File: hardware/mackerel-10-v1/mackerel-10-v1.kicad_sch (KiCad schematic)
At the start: 14 parts, among them J1 Conn_02x05_Odd_Even, J2 DIN41612_02x32_AC, U1 68010D, X1 50 MHz

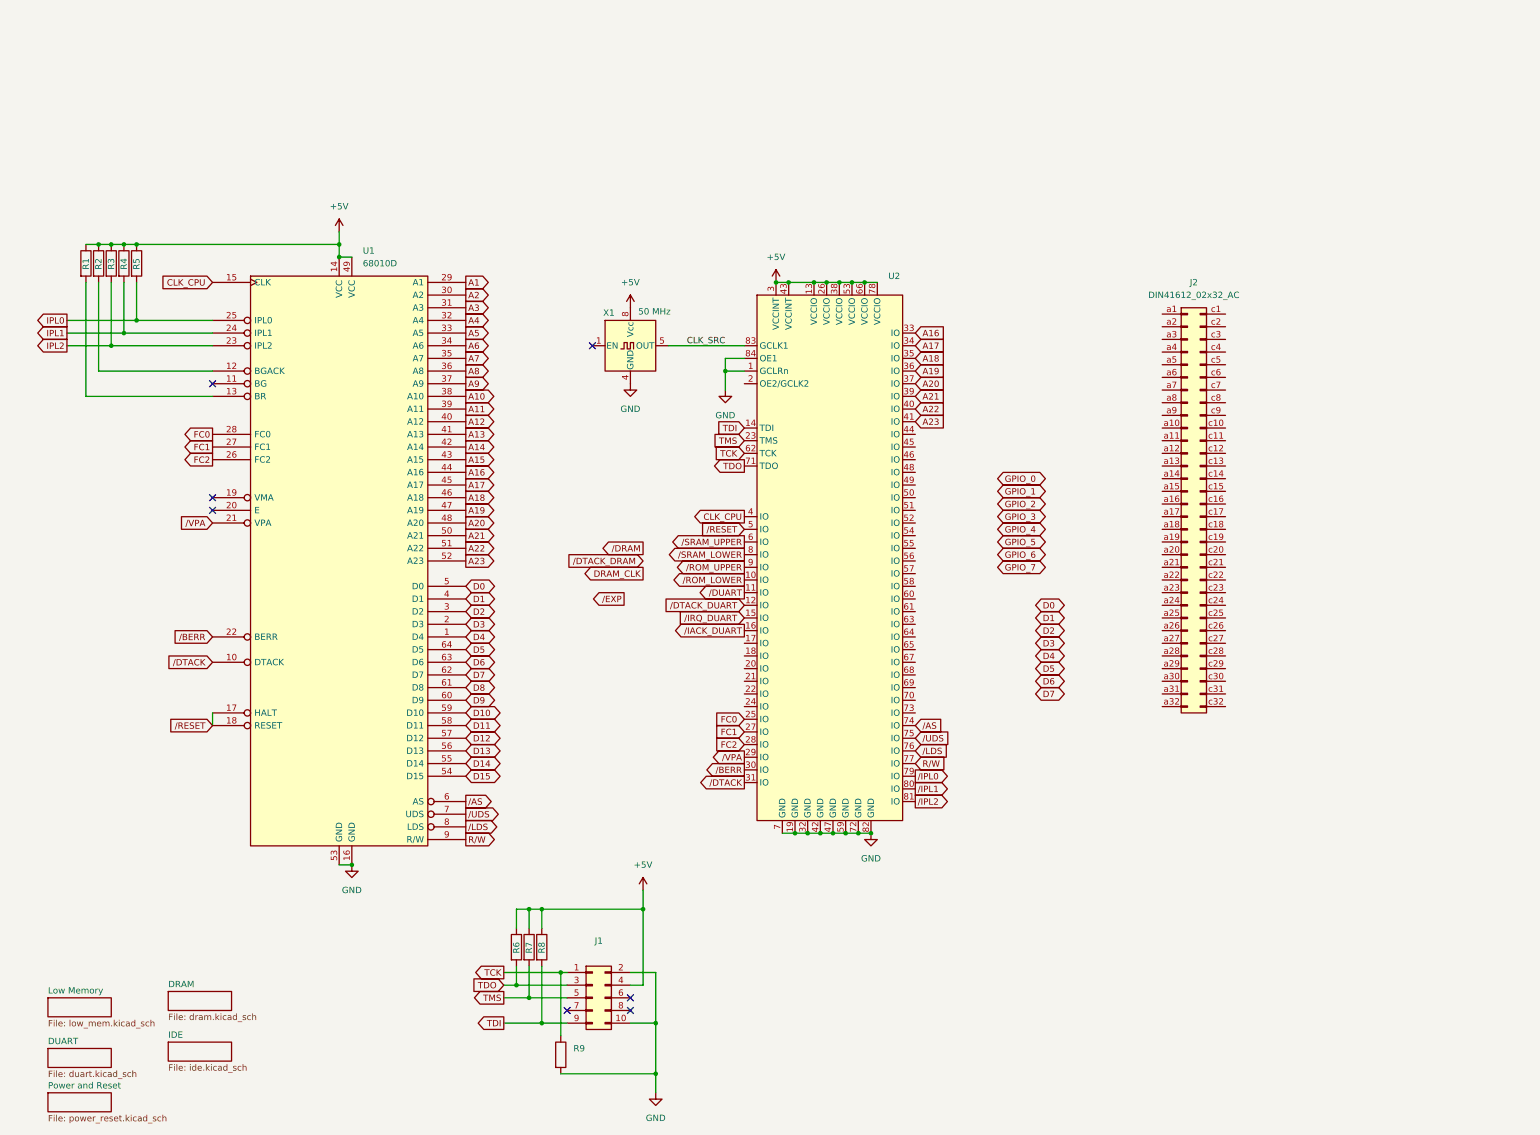
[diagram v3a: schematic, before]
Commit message: Rough layout of simplified Mack-10 prototype
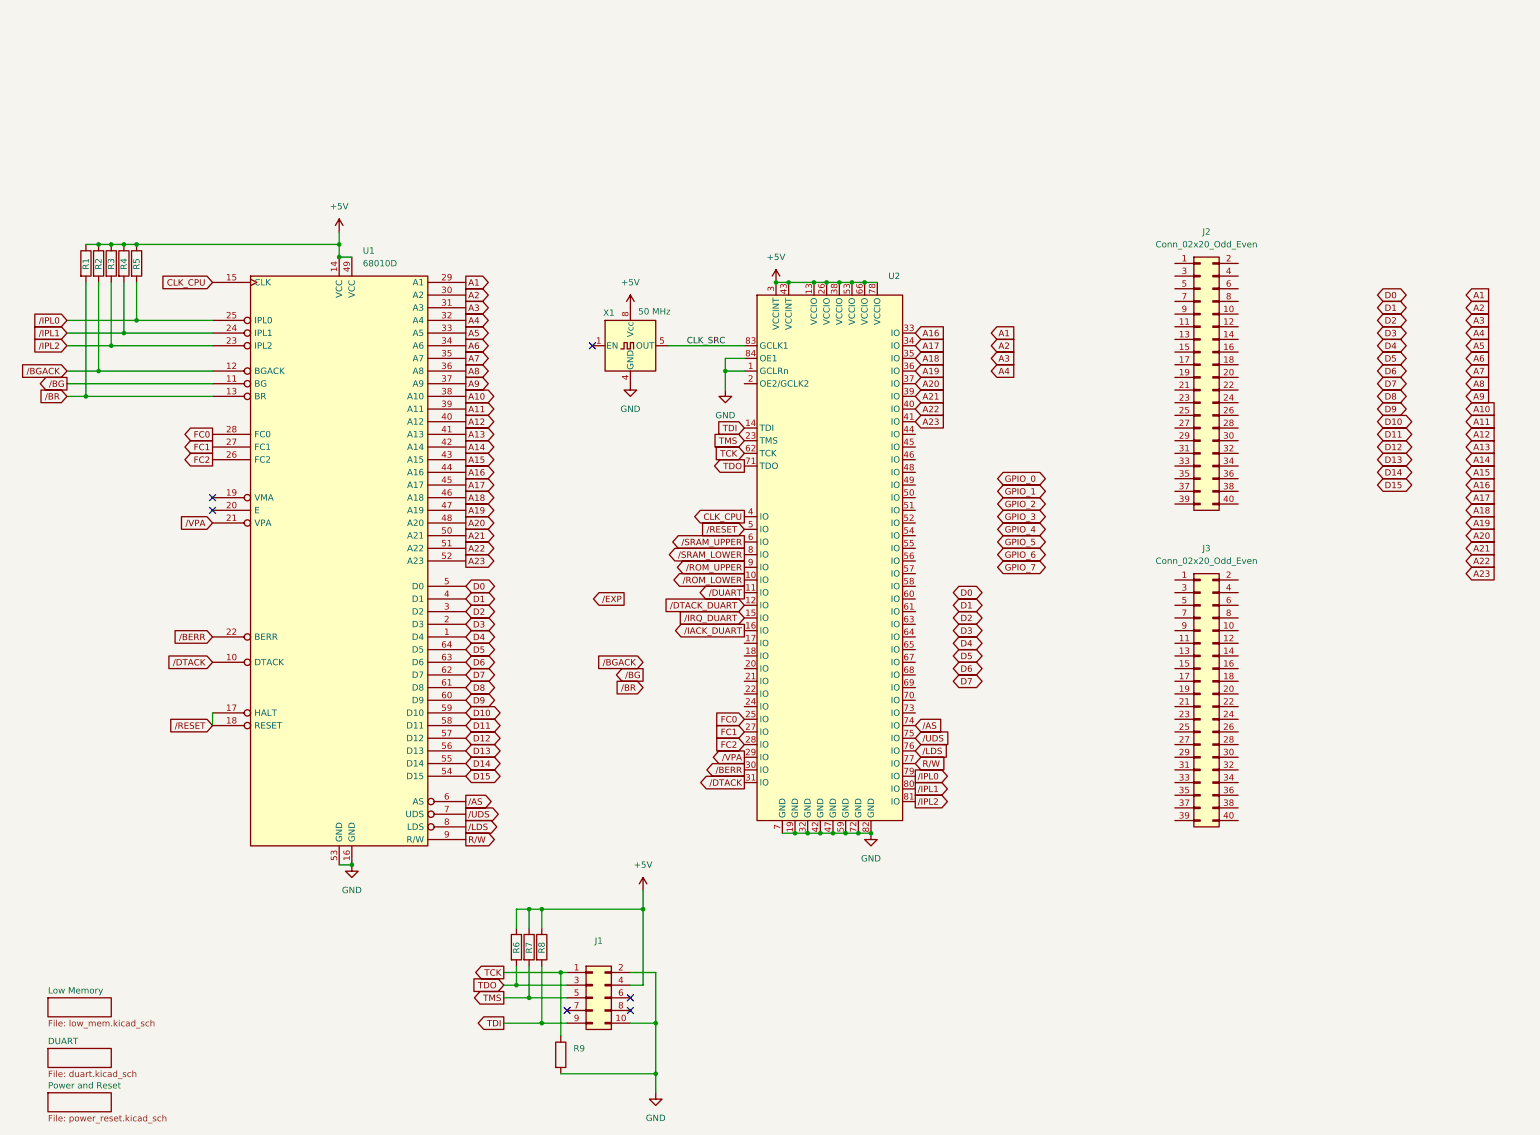
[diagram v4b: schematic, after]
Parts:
- removed J2: DIN41612_02x32_AC, Connector_DIN:DIN41612_C_2x32_Female_Vertical_THT, symbol Connector:DIN41612_02x32_AC
- added J2, J3: Conn_02x20_Odd_Even, Connector_IDC:IDC-Header_2x20_P2.54mm_Vertical, symbol Connector_Generic:Conn_02x20_Odd_Even
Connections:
- net IPL0 is gone; now on net /IPL0: R5.2, U1.25 (IPL0)
- net IPL1 is gone; now on net /IPL1: R4.2, U1.24 (IPL1)
- net IPL2 is gone; now on net /IPL2: R3.2, U1.23 (IPL2)
- net /BG: now reaches U1.11 (BG)
- net /BGACK: now reaches R2.2, U1.12 (BGACK)
- net /BR: now reaches R1.2, U1.13 (BR)
- no-connect marks 7 -> 6
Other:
- removed sheet DRAM
- removed sheet IDE

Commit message: Mack-10 proto routed except for expansion headers
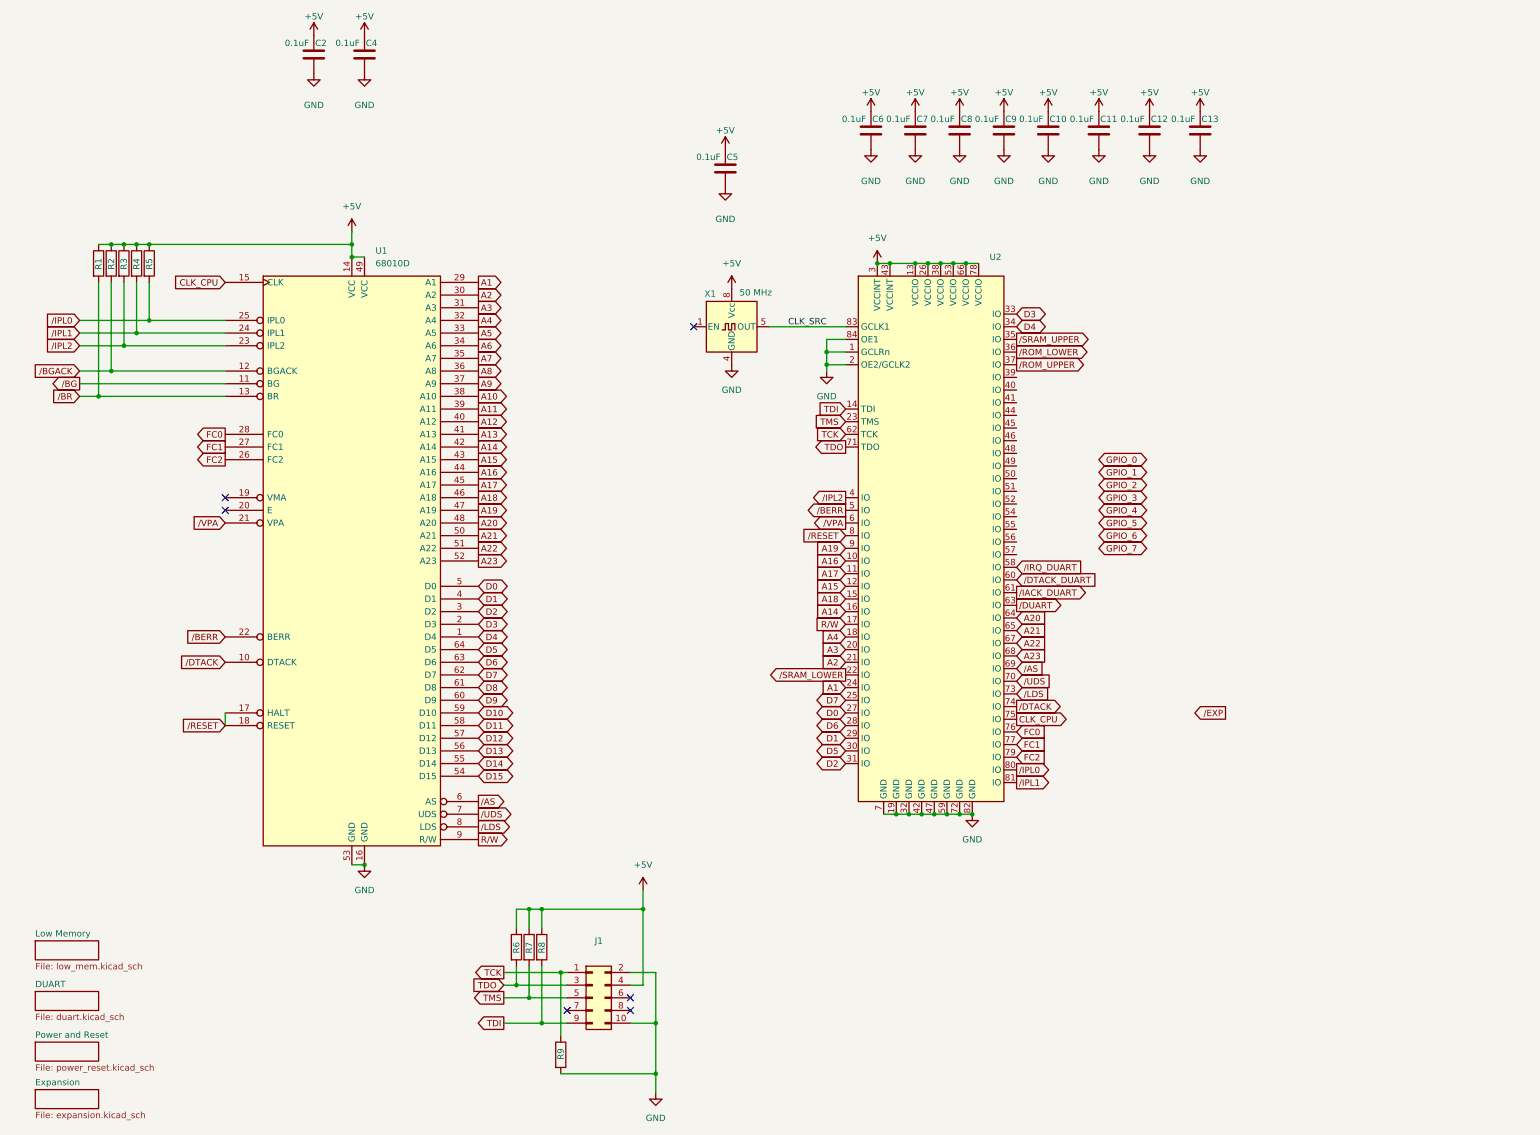
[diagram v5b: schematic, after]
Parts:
- removed J2, J3: Conn_02x20_Odd_Even, Connector_IDC:IDC-Header_2x20_P2.54mm_Vertical, symbol Connector_Generic:Conn_02x20_Odd_Even
- added C10, C11, C12, C13, C2, C4, C5, C6, C7, C8, C9: 0.1uF, Capacitor_THT:C_Disc_D4.7mm_W2.5mm_P5.00mm, symbol Device:C
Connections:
- net +5V: now also C10.1, C11.1, C12.1, C13.1, C2.1, C4.1, C5.1, C6.1, C7.1, C8.1, C9.1
- net A1: now also U2.24 (IO)
- net A14: now also U2.16 (IO)
- net A15: now also U2.12 (IO)
- net A16: now also U2.10 (IO); no longer U2.33 (IO)
- net A17: now also U2.11 (IO); no longer U2.34 (IO)
- net A18: now also U2.15 (IO); no longer U2.35 (IO)
- net A19: now also U2.9 (IO); no longer U2.36 (IO)
- net A2: now also U2.21 (IO)
- net A20: now also U2.64 (IO); no longer U2.37 (IO)
- net A21: now also U2.65 (IO); no longer U2.39 (IO)
- net A22: now also U2.67 (IO); no longer U2.40 (IO)
- net A23: now also U2.68 (IO); no longer U2.41 (IO)
- net A3: now also U2.20 (IO)
- net A4: now also U2.18 (IO)
- net CLK_CPU: now also U2.75 (IO); no longer U2.4 (IO)
- net D0: now also U2.27 (IO)
- net D1: now also U2.29 (IO)
- net D2: now also U2.31 (IO)
- net D3: now also U2.33 (IO)
- net D4: now also U2.34 (IO)
- net D5: now also U2.30 (IO)
- net D6: now also U2.28 (IO)
- net D7: now also U2.25 (IO)
- net FC0: now also U2.76 (IO); no longer U2.25 (IO)
- net FC1: now also U2.77 (IO); no longer U2.27 (IO)
- net FC2: now also U2.79 (IO); no longer U2.28 (IO)
- net GND: now also U2.2 (OE2/GCLK2), C10.2, C11.2, C12.2, C13.2, C2.2, C4.2, C5.2, C6.2, C7.2, C8.2, C9.2
- net R/W: now also U2.17 (IO); no longer U2.77 (IO)
- net /AS: now also U2.69 (IO); no longer U2.74 (IO)
- net /BERR: now also U2.5 (IO); no longer U2.30 (IO)
- net /DTACK: now also U2.74 (IO); no longer U2.31 (IO)
- net /DTACK_DUART: now also U2.60 (IO); no longer U2.12 (IO)
- net /DUART: now also U2.63 (IO); no longer U2.11 (IO)
- net /IACK_DUART: now also U2.61 (IO); no longer U2.16 (IO)
- net /IPL0: now also U2.80 (IO); no longer U2.79 (IO)
- net /IPL1: now also U2.81 (IO); no longer U2.80 (IO)
- net /IPL2: now also U2.4 (IO); no longer U2.81 (IO)
- net /IRQ_DUART: now also U2.58 (IO); no longer U2.15 (IO)
- net /LDS: now also U2.73 (IO); no longer U2.76 (IO)
- net /RESET: now also U2.8 (IO); no longer U2.5 (IO)
- net /ROM_LOWER: now also U2.36 (IO); no longer U2.10 (IO)
- net /ROM_UPPER: now also U2.37 (IO); no longer U2.9 (IO)
- net /SRAM_LOWER: now also U2.22 (IO); no longer U2.8 (IO)
- net /SRAM_UPPER: now also U2.35 (IO); no longer U2.6 (IO)
- net /UDS: now also U2.70 (IO); no longer U2.75 (IO)
- net /VPA: now also U2.6 (IO); no longer U2.29 (IO)
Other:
- added sheet Expansion (expansion.kicad_sch)
- moved on the sheet: R1, R2, R3, R4, R5, U1, U2, X1

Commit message: Mack-10 proto fully routed
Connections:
- net GPIO_0: now also U2.46 (IO)
- net GPIO_1: now also U2.45 (IO)
- net GPIO_2: now also U2.48 (IO)
- net GPIO_3: now also U2.49 (IO)
- net GPIO_4: now also U2.50 (IO)
- net GPIO_5: now also U2.51 (IO)
- net GPIO_6: now also U2.52 (IO)
- net GPIO_7: now also U2.54 (IO)
- net /EXP: now also U2.40 (IO)
- net /IRQ_EXP: now reaches U2.39 (IO)
- net /IACK_EXP: now reaches U2.41 (IO)
- net /DTACK_EXP: now reaches U2.44 (IO)
- net /BG: no longer names the net of U1.11 (BG)
- net /BGACK: no longer names the net of R2.2, U1.12 (BGACK)
- net /BR: no longer names the net of R1.2, U1.13 (BR)
- no-connect marks 6 -> 9
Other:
- note added: "TODO: extra chip select, DTACK, and IRQ/IACK pins"
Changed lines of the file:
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@@
 	)
 	(junction
+		(at 177.8 40.64)
+		(diameter 0)
+		(color 0 0 0 0)
+	)
+	(junction
 		(at 191.77 27.94)
 		(diameter 0)
@@
 	)
 	(no_connect
+		(at 212.09 86.36)
+	)
+	(no_connect
+		(at 212.09 81.28)
+	)
+	(no_connect
 		(at 134.62 175.26)
 	)
@@
 		(at 121.92 177.8)
 	)
+	(no_connect
+		(at 212.09 83.82)
+	)
 	(wire
 		(pts
@@
 	(wire
 		(pts
-			(xy 24.13 52.07) (xy 53.34 52.07)
+			(xy 33.02 44.45) (xy 53.34 44.45)
 		)
 		(stroke
@@
 	(wire
 		(pts
-			(xy 33.02 44.45) (xy 53.34 44.45)
+			(xy 198.12 138.43) (xy 200.66 138.43)
 		)
 		(stroke
@@
 	(wire
 		(pts
-			(xy 198.12 138.43) (xy 200.66 138.43)
+			(xy 109.22 175.26) (xy 114.3 175.26)
 		)
 		(stroke
@@
 	(wire
 		(pts
-			(xy 109.22 175.26) (xy 114.3 175.26)
+			(xy 173.99 36.83) (xy 177.8 36.83)
 		)
 		(stroke
@@
 	(wire
 		(pts
+			(xy 177.8 36.83) (xy 177.8 40.64)
+		)
+		(stroke
+			(width 0)
+			(type default)
+		)
+	)
+	(wire
+		(pts
 			(xy 24.13 39.37) (xy 38.1 39.37)
 		)
@@
 		)
 	)
-	(label "CLK_SRC"
-		(at 173.99 40.64 180)
-		(fields_autoplaced yes)
+	(text "TODO: extra chip select, DTACK, and IRQ/IACK pins"
+		(exclude_from_sim no)
+		(at 284.734 38.862 0)
 		(effects
 			(font
 				(size 1.27 1.27)
 			)
-			(justify right bottom)
 		)
 	)
@@
 		)
 	)
-	(global_label "{slash}BG"
-		(shape output)
-		(at 24.13 52.07 180)
-		(fields_autoplaced yes)
-		(effects
-			(font
-				(size 1.27 1.27)
-			)
-			(justify right)
-		)
-		(property "Intersheetrefs" "${INTERSHEET_REFS}"
-			(at 17.2743 52.07 0)
-			(effects
-				(font
-					(size 1.27 1.27)
-				)
-				(justify right)
-				(hide yes)
-			)
-		)
-	)
 	(global_label "A16"
 		(shape output)
@@
 	(global_label "GPIO_0"
 		(shape bidirectional)
-		(at 228.6 67.31 0)
+		(at 212.09 63.5 0)
 		(fields_autoplaced yes)
 		(effects
@@
 		)
 		(property "Intersheetrefs" "${INTERSHEET_REFS}"
-			(at 239.3489 67.31 0)
+			(at 222.8389 63.5 0)
 			(effects
 				(font
@@
 		)
 	)
-	(global_label "{slash}BGACK"
-		(shape input)
-		(at 24.13 49.53 180)
-		(fields_autoplaced yes)
-		(effects
-			(font
-				(size 1.27 1.27)
-			)
-			(justify right)
-		)
-		(property "Intersheetrefs" "${INTERSHEET_REFS}"
-			(at 13.6457 49.53 0)
-			(effects
-				(font
-					(size 1.27 1.27)
-				)
-				(justify right)
-				(hide yes)
-			)
-		)
-	)
 	(global_label "{slash}UDS"
 		(shape output)
@@
 	(global_label "GPIO_4"
 		(shape bidirectional)
-		(at 228.6 77.47 0)
+		(at 212.09 71.12 0)
 		(fields_autoplaced yes)
 		(effects
@@
 		)
 		(property "Intersheetrefs" "${INTERSHEET_REFS}"
-			(at 239.3489 77.47 0)
+			(at 222.8389 71.12 0)
 			(effects
 				(font
@@
 		)
 	)
+	(global_label "{slash}DTACK_EXP"
+		(shape input)
+		(at 212.09 58.42 0)
+		(fields_autoplaced yes)
+		(effects
+			(font
+				(size 1.27 1.27)
+			)
+			(justify left)
+		)
+		(property "Intersheetrefs" "${INTERSHEET_REFS}"
+			(at 226.868 58.42 0)
+			(effects
+				(font
+					(size 1.27 1.27)
+				)
+				(justify left)
+				(hide yes)
+			)
+		)
+	)
 	(global_label "FC1"
 		(shape output)
@@
 	(global_label "GPIO_7"
 		(shape bidirectional)
-		(at 228.6 85.09 0)
+		(at 212.09 78.74 0)
 		(fields_autoplaced yes)
 		(effects
@@
 		)
 		(property "Intersheetrefs" "${INTERSHEET_REFS}"
-			(at 239.3489 85.09 0)
+			(at 222.8389 78.74 0)
 			(effects
 				(font
@@
 		)
 	)
-	(global_label "{slash}EXP"
-		(shape output)
-		(at 254 118.11 180)
-		(fields_autoplaced yes)
-		(effects
-			(font
-				(size 1.27 1.27)
-			)
-			(justify right)
-		)
-		(property "Intersheetrefs" "${INTERSHEET_REFS}"
-			(at 246.0558 118.11 0)
-			(effects
-				(font
-					(size 1.27 1.27)
-				)
-				(justify right)
-				(hide yes)
-			)
-		)
-	)
 	(global_label "{slash}UDS"
 		(shape input)
@@
 	(global_label "GPIO_6"
 		(shape bidirectional)
-		(at 228.6 82.55 0)
+		(at 212.09 76.2 0)
 		(fields_autoplaced yes)
 		(effects
@@
 		)
 		(property "Intersheetrefs" "${INTERSHEET_REFS}"
-			(at 239.3489 82.55 0)
+			(at 222.8389 76.2 0)
 			(effects
 				(font
@@
 	(global_label "GPIO_3"
 		(shape bidirectional)
-		(at 228.6 74.93 0)
+		(at 212.09 68.58 0)
 		(fields_autoplaced yes)
 		(effects
@@
 		)
 		(property "Intersheetrefs" "${INTERSHEET_REFS}"
-			(at 239.3489 74.93 0)
+			(at 222.8389 68.58 0)
 			(effects
 				(font
@@
 		)
 	)
+	(global_label "{slash}IACK_EXP"
+		(shape output)
+		(at 212.09 55.88 0)
+		(fields_autoplaced yes)
+		(effects
+			(font
+				(size 1.27 1.27)
+			)
+			(justify left)
+		)
+		(property "Intersheetrefs" "${INTERSHEET_REFS}"
+			(at 225.2352 55.88 0)
+			(effects
+				(font
+					(size 1.27 1.27)
+				)
+				(justify left)
+				(hide yes)
+			)
+		)
+	)
 	(global_label "{slash}VPA"
 		(shape output)
@@
 		)
 	)
+	(global_label "{slash}IRQ_EXP"
+		(shape input)
+		(at 212.09 50.8 0)
+		(fields_autoplaced yes)
+		(effects
+			(font
+				(size 1.27 1.27)
+			)
+			(justify left)
+		)
+		(property "Intersheetrefs" "${INTERSHEET_REFS}"
+			(at 224.2071 50.8 0)
+			(effects
+				(font
+					(size 1.27 1.27)
+				)
+				(justify left)
+				(hide yes)
+			)
+		)
+	)
 	(global_label "A13"
 		(shape output)
@@
 	(global_label "GPIO_1"
 		(shape bidirectional)
-		(at 228.6 69.85 0)
+		(at 212.09 60.96 0)
 		(fields_autoplaced yes)
 		(effects
@@
 		)
 		(property "Intersheetrefs" "${INTERSHEET_REFS}"
-			(at 239.3489 69.85 0)
+			(at 222.8389 60.96 0)
 			(effects
 				(font
@@
 		)
 	)
+	(global_label "{slash}EXP"
+		(shape output)
+		(at 212.09 53.34 0)
+		(fields_autoplaced yes)
+		(effects
+			(font
+				(size 1.27 1.27)
+			)
+			(justify left)
+		)
+		(property "Intersheetrefs" "${INTERSHEET_REFS}"
+			(at 220.0342 53.34 0)
+			(effects
+				(font
+					(size 1.27 1.27)
+				)
+				(justify left)
+				(hide yes)
+			)
+		)
+	)
 	(global_label "A4"
 		(shape output)
@@
 	(global_label "GPIO_5"
 		(shape bidirectional)
-		(at 228.6 80.01 0)
+		(at 212.09 73.66 0)
 		(fields_autoplaced yes)
 		(effects
@@
 		)
 		(property "Intersheetrefs" "${INTERSHEET_REFS}"
-			(at 239.3489 80.01 0)
+			(at 222.8389 73.66 0)
 			(effects
 				(font
@@
 	(global_label "GPIO_2"
 		(shape bidirectional)
-		(at 228.6 72.39 0)
+		(at 212.09 66.04 0)
 		(fields_autoplaced yes)
 		(effects
@@
 		)
 		(property "Intersheetrefs" "${INTERSHEET_REFS}"
-			(at 239.3489 72.39 0)
+			(at 222.8389 66.04 0)
 			(effects
 				(font
@@
 		)
 	)
-	(global_label "{slash}BR"
-		(shape input)
-		(at 24.13 54.61 180)
+	(global_label "D2"
+		(shape bidirectional)
+		(at 177.8 128.27 180)
 		(fields_autoplaced yes)
 		(effects
@@
 		)
 		(property "Intersheetrefs" "${INTERSHEET_REFS}"
-			(at 17.2743 54.61 0)
+			(at 171.224 128.27 0)
 			(effects
 				(font
@@
 		)
 	)
-	(global_label "D2"
-		(shape bidirectional)
-		(at 177.8 128.27 180)
+	(global_label "A5"
+		(shape output)
+		(at 104.14 41.91 0)
 		(fields_autoplaced yes)
 		(effects
@@
 				(size 1.27 1.27)
 			)
-			(justify right)
+			(justify left)
 		)
 		(property "Intersheetrefs" "${INTERSHEET_REFS}"
-			(at 171.224 128.27 0)
+			(at 109.4233 41.91 0)
 			(effects
 				(font
 					(size 1.27 1.27)
 				)
-				(justify right)
+				(justify left)
 				(hide yes)
 			)
 		)
 	)
-	(global_label "A5"
-		(shape output)
-		(at 104.14 41.91 0)
+	(global_label "CLK_SRC"
+		(shape input)
+		(at 173.99 36.83 180)
 		(fields_autoplaced yes)
 		(effects
@@
 				(size 1.27 1.27)
 			)
-			(justify left)
+			(justify right)
 		)
 		(property "Intersheetrefs" "${INTERSHEET_REFS}"
-			(at 109.4233 41.91 0)
+			(at 162.7196 36.83 0)
 			(effects
 				(font
 					(size 1.27 1.27)
 				)
-				(justify left)
+				(justify right)
 				(hide yes)
 			)
